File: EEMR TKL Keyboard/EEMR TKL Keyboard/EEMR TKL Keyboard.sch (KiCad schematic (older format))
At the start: 190 parts

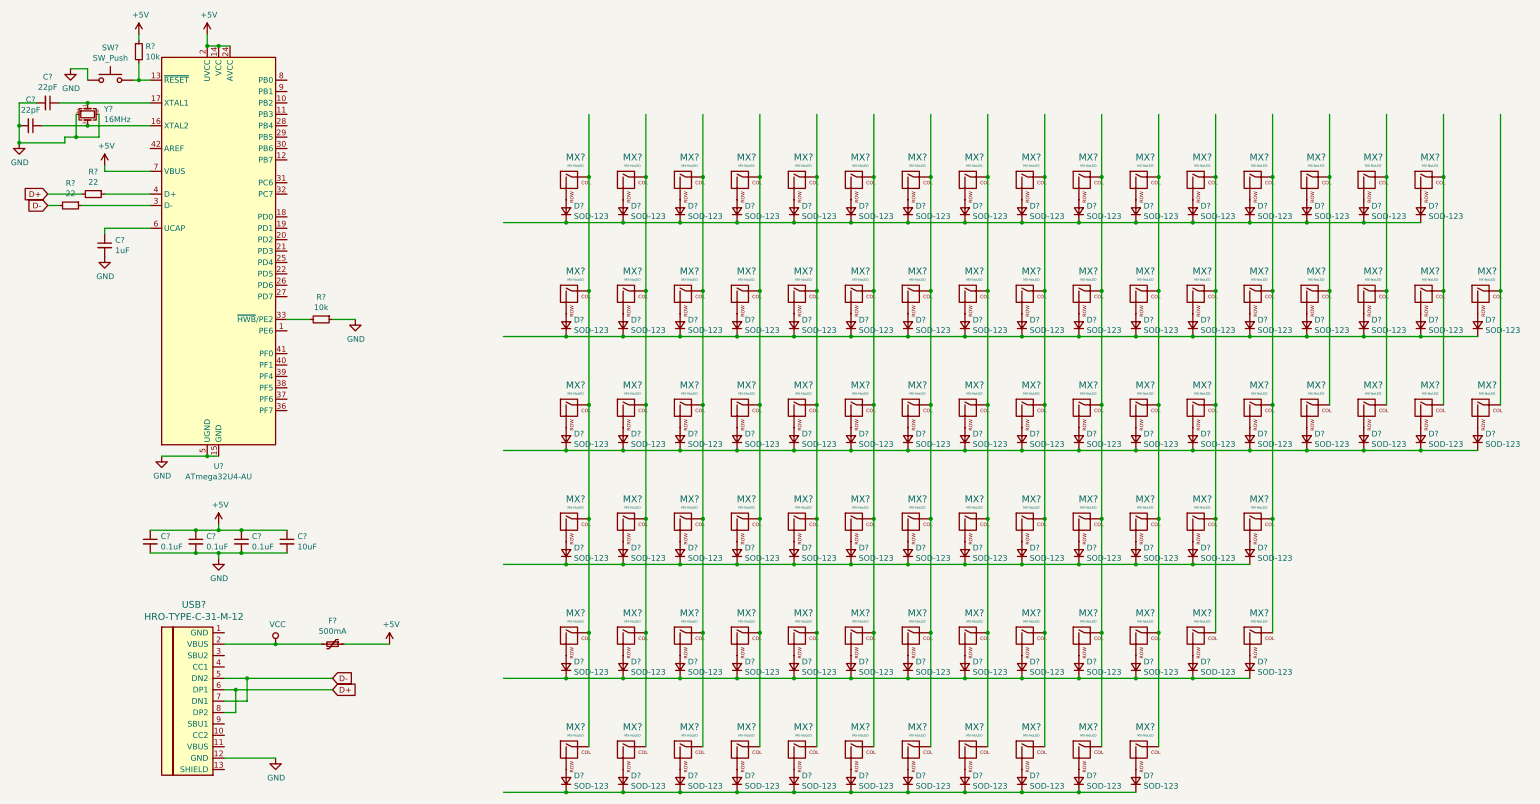
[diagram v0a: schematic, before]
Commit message: completed schematic for tkl
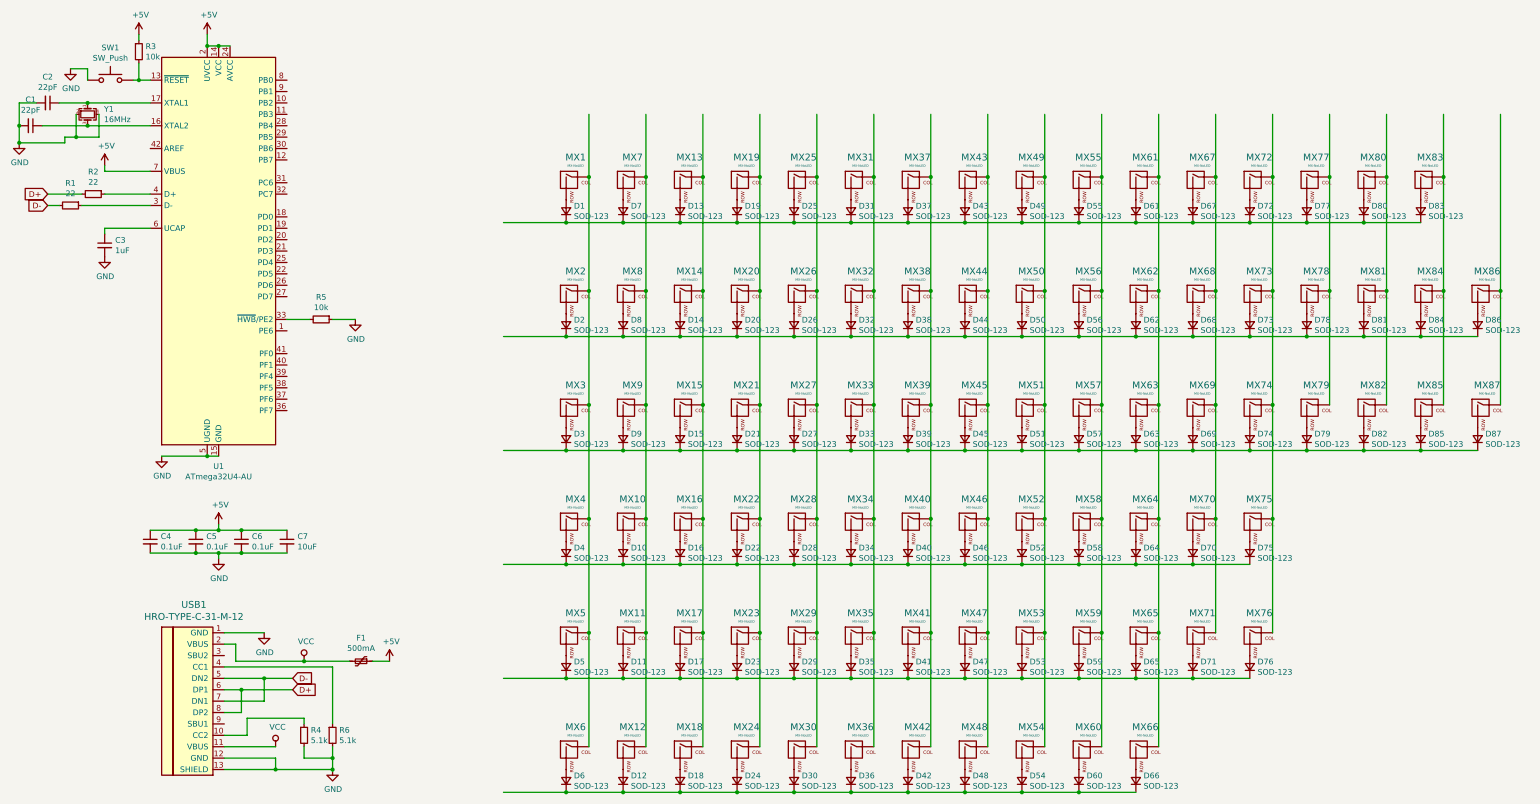
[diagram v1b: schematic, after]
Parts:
- added R4, R6: 5.1k, symbol Device:R_Small
- gave numbers to parts that had none: 190
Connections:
- wire segments 230 -> 247
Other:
- moved on the sheet: F1
